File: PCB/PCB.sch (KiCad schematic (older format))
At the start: 151 parts

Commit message: Updated the PCB schematic.
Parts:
- removed D? (x8): 1N4148, symbol Device:D_Small_ALT
- removed SW?: SW_0-12, symbol Switch:SW_MEC_5G
- removed SW? (x3): SW_0-13, symbol Switch:SW_MEC_5G
- removed SW?: SW_0-2, symbol Switch:SW_MEC_5G
- removed SW?: SW_0-3, symbol Switch:SW_MEC_5G
- removed SW?: SW_0-5, symbol Switch:SW_MEC_5G
- removed SW?: SW_0-6, symbol Switch:SW_MEC_5G
- removed SW?: SW_0-7, symbol Switch:SW_MEC_5G
- added OL?: SSD1306, symbol kbd:OLED
- added SW?: ENCODER, symbol Device:Rotary_Encoder_Switch
- SW?: value SW_0-0 -> SW_1-0
- SW?: value SW_0-1 -> SW_1-1
- SW?: value SW_0-2 -> SW_1-2
- SW?: value SW_0-3 -> SW_1-3
- SW?: value SW_0-4 -> SW_1-4
- SW?: value SW_0-5 -> SW_1-5
- SW?: value SW_0-6 -> SW_1-6
- SW?: value SW_0-7 -> SW_1-7
- SW?: value SW_0-8 -> SW_1-8
- SW?: value SW_0-9 -> SW_1-9
- SW?: value SW_0-10 -> SW_1-10
- SW?: value SW_0-11 -> SW_1-11
- SW?: value SW_0-12 -> SW_1-12
- SW?: value SW_0-13 -> SW_1-13
- SW?: value SW_0-14 -> SW_1-14
- SW?: value SW_0-0 -> SW_2-0
- SW?: value SW_0-1 -> SW_2-1
- SW?: value SW_0-2 -> SW_2-2
- SW?: value SW_0-3 -> SW_2-3
- SW?: value SW_0-4 -> SW_2-4
- SW?: value SW_0-5 -> SW_2-5
- SW?: value SW_0-6 -> SW_2-6
- SW?: value SW_0-7 -> SW_2-7
- SW?: value SW_0-8 -> SW_2-8
- SW?: value SW_0-9 -> SW_2-9
- SW?: value SW_0-10 -> SW_2-10
- SW?: value SW_0-11 -> SW_2-11
- SW?: value SW_0-14 -> SW_2-14
- SW?: value SW_0-0 -> SW_3-0
- SW?: value SW_0-1 -> SW_3-1
- SW?: value SW_0-2 -> SW_3-3
- SW?: value SW_0-3 -> SW_3-3
- SW?: value SW_0-4 -> SW_3-4
- SW?: value SW_0-5 -> SW_3-5
- SW?: value SW_0-6 -> SW_3-6
- SW?: value SW_0-7 -> SW_3-7
- SW?: value SW_0-8 -> SW_3-8
- SW?: value SW_0-9 -> SW_3-9
- SW?: value SW_0-10 -> SW_3-10
- SW?: value SW_0-11 -> SW_3-11
- SW?: value SW_0-12 -> SW_3-12
- SW?: value SW_0-14 -> SW_3-14
- SW?: value SW_0-0 -> SW_4-0
- SW?: value SW_0-1 -> SW_4-1
- SW?: value SW_0-4 -> SW_4-4
- SW?: value SW_0-8 -> SW_4-8
- SW?: value SW_0-9 -> SW_4-9
- SW?: value SW_0-10 -> SW_4-10
- SW?: value SW_0-11 -> SW_4-11
- SW?: value SW_0-12 -> SW_4-12
- SW?: value SW_0-14 -> SW_4-14
- U?: value YAAJ_BlackPill_Part_Like -> STM32 BlackPill
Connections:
- net COL0: now also U?.19 (PB8)
- net COL1: now also U?.20 (PB9)
- net COL10: now also U?.31 (PB0)
- net COL11: now also U?.32 (PB1)
- net COL12: now also U?.33 (PB10)
- net COL13: now also U?.34 (PB11), SW?.S1
- net COL14: now also U?.6 (PA9)
- net COL2: now also U?.23 (PA0)
- net COL3: now also U?.24 (PA1)
- net COL4: now also U?.25 (PA2)
- net COL5: now also U?.26 (PA3)
- net COL6: now also U?.27 (PA4)
- net COL7: now also U?.28 (PA5)
- net COL8: now also U?.29 (PA6)
- net COL9: now also U?.30 (PA7)
- net ROW0: now also U?.13 (PB5)
- net ROW1: now also U?.12 (PB4)
- net ROW2: now also U?.11 (PB3); no longer D?.1 (K)
- net ROW3: now also D?.1 (K), U?.10 (PA15)
- net ROW4: now also U?.7 (PA10)
- net at U?.14 (PB6): now also OL?.2 (SCL)
- net at U?.15 (PB7): now also OL?.1 (SDA)
- net at U?.16 (3V3): now also OL?.3 (VCC)
- net at U?.17 (GND): now also OL?.4 (GND)
- net at U?.2 (PB13): now also SW?.B
- net at U?.3 (PB14): now also SW?.C
- net at U?.4 (PB15): now also SW?.A
- net at D?.2 (A): now also SW?.S2
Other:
- moved on the sheet: D?, SW?, U?

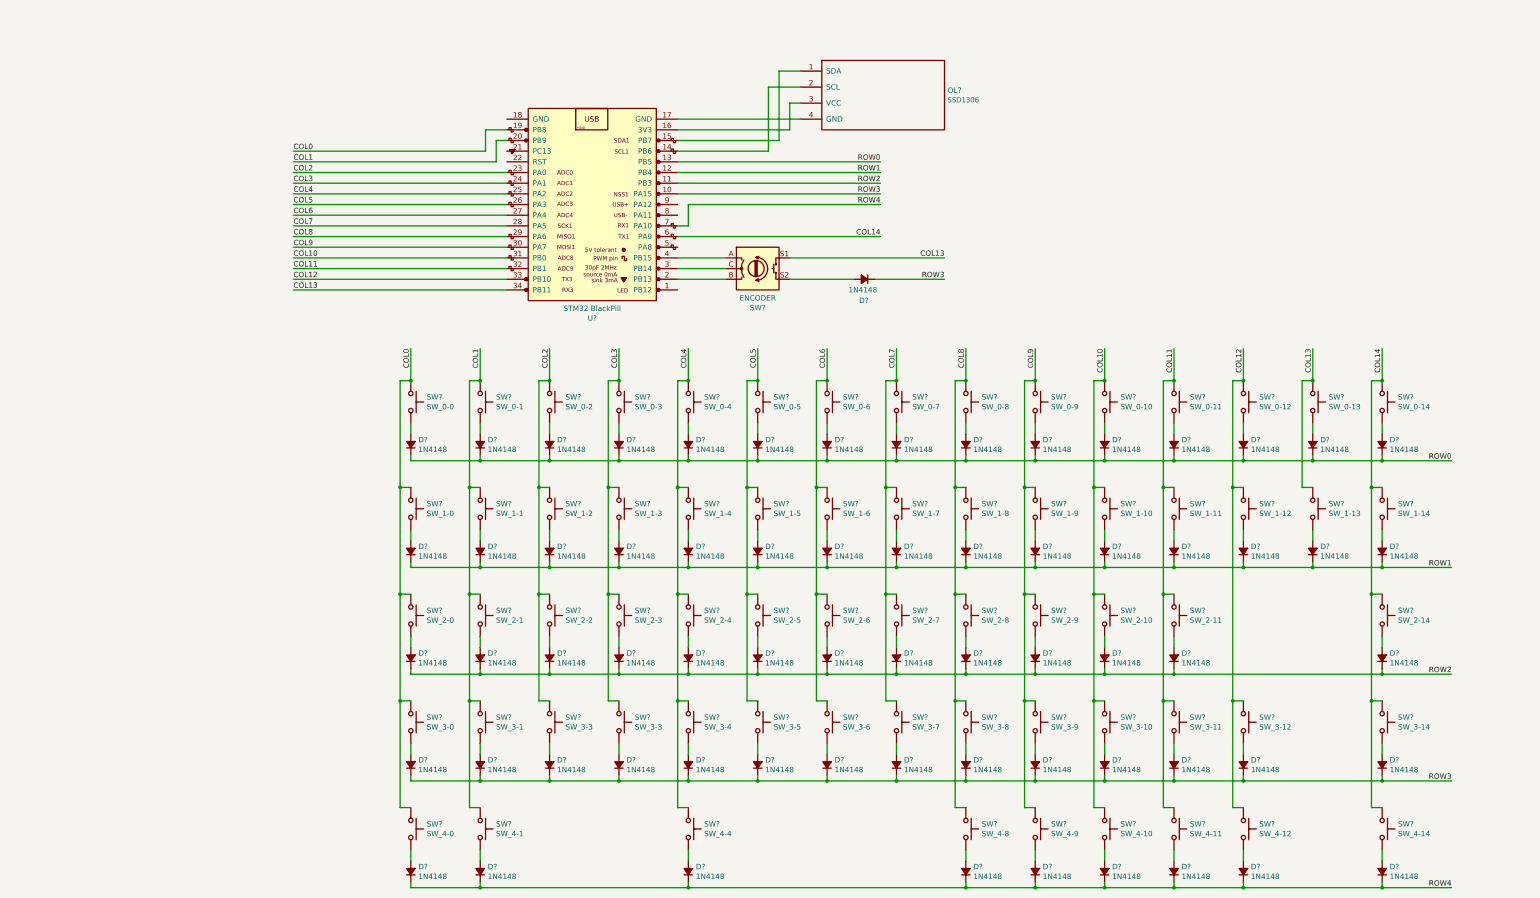
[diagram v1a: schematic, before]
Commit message: Updated the schematic, which should now be finished.
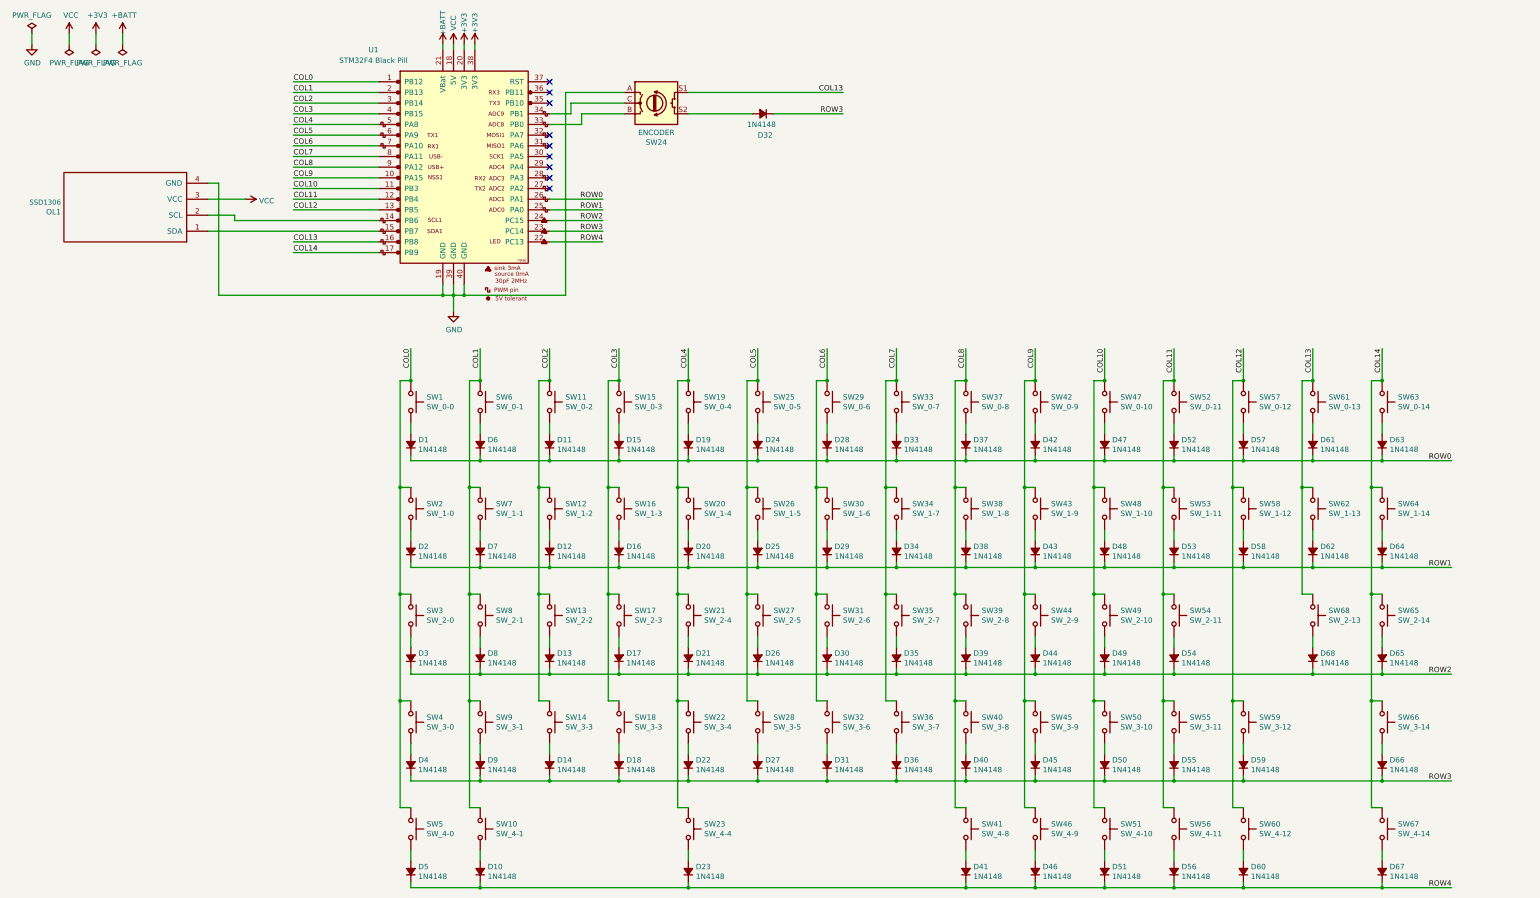
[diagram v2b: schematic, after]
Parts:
- removed U?: STM32 BlackPill, symbol YAAJ_BlackPill_Part_Like:YAAJ_BlackPill_Part_Like
- added D68: 1N4148, Diode_THT:D_DO-201_P12.70mm_Horizontal, symbol Device:D_Small_ALT
- added SW68: SW_2-13, Button_Switch_Keyboard:SW_Cherry_MX_2.25u_PCB, symbol Switch:SW_MEC_5G
- added U1: STM32F4 Black Pill, Footprints:YAAJ_BluePill_SWD_1, symbol YAAJ_BluePill:YAAJ_BluePill
- D1, D10, D11, D12, D13, D14, D15, D16, D17, D18, D19, D2, D20, D21, D22, D23, D24, D25, D26, D27, D28, D29, D3, D30, D31, D32, D33, D34, D35, D36, D37, D38, D39, D4, D40, D41, D42, D43, D44, D45, D46, D47, D48, D49, D5, D50, D51, D52, D53, D54, D55, D56, D57, D58, D59, D6, D60, D61, D62, D63, D64, D65, D66, D67, D7, D8, D9: renamed from D?; footprint (none) -> Diode_THT:D_DO-201_P12.70mm_Horizontal
- OL1: renamed from OL?; footprint (none) -> Connector_PinHeader_2.54mm:PinHeader_1x04_P2.54mm_Vertical
- SW1, SW10, SW11, SW12, SW13, SW14, SW15, SW16, SW17, SW18, SW19, SW20, SW21, SW22, SW25, SW26, SW27, SW28, SW29, SW30, SW31, SW32, SW33, SW34, SW35, SW36, SW37, SW38, SW39, SW40, SW42, SW43, SW44, SW45, SW47, SW48, SW49, SW50, SW52, SW53, SW54, SW56, SW57, SW58, SW59, SW6, SW60, SW63, SW64, SW65, SW66, SW67, SW7, SW8, SW9: renamed from SW?; footprint (none) -> Button_Switch_Keyboard:SW_Cherry_MX_1.00u_PCB
- SW2, SW5, SW62: renamed from SW?; footprint (none) -> Button_Switch_Keyboard:SW_Cherry_MX_1.50u_PCB
- SW23: renamed from SW?; footprint (none) -> Button_Switch_Keyboard:SW_Cherry_MX_6.25u_PCB
- SW24: renamed from SW?; footprint (none) -> Rotary_Encoder:RotaryEncoder_Alps_EC11E_Vertical_H20mm
- SW3, SW55: renamed from SW?; footprint (none) -> Button_Switch_Keyboard:SW_Cherry_MX_1.75u_PCB
- SW4: renamed from SW?; footprint (none) -> Button_Switch_Keyboard:SW_Cherry_MX_2.25u_PCB
- SW41, SW46, SW51: renamed from SW?; footprint (none) -> Button_Switch_Keyboard:SW_Cherry_MX_1.25u_PCB
- SW61: renamed from SW?; footprint (none) -> Button_Switch_Keyboard:SW_Cherry_MX_2.00u_PCB
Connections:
- net COL0: now also U1.1 (PB12)
- net COL1: now also U1.2 (PB13)
- net COL10: now also U1.11 (PB3)
- net COL11: now also U1.12 (PB4)
- net COL12: now also U1.13 (PB5)
- net COL13: now also SW68.1 (A), SW68.2 (A), U1.16 (PB8)
- net COL14: now also U1.17 (PB9)
- net COL2: now also U1.3 (PB14)
- net COL3: now also U1.4 (PB15)
- net COL4: now also U1.5 (PA8)
- net COL5: now also U1.6 (PA9)
- net COL6: now also U1.7 (PA10)
- net COL7: now also U1.8 (PA11)
- net COL8: now also U1.9 (PA12)
- net COL9: now also U1.10 (PA15)
- net ROW0: now also U1.26 (PA1)
- net ROW1: now also U1.25 (PA0)
- net ROW2: now also D68.1 (K), U1.24 (PC15)
- net ROW3: now also U1.23 (PC14)
- net ROW4: now also U1.22 (PC13)
- net at OL1.2 (SCL): now also U1.14 (PB6)
- net at OL1.1 (SDA): now also U1.15 (PB7)
- net VCC: now reaches OL1.3 (VCC)
- net VCC: now also U1.18 (5V)
- net GND: now reaches OL1.4 (GND)
- net GND: now also SW24.A, U1.19 (GND), U1.39 (GND), U1.40 (GND)
- net at SW24.B: now also U1.33 (PB0)
- net at SW24.C: now also U1.34 (PB1)
- new net: D68.2 (A), SW68.3 (B), SW68.4 (B)
- new net +3V3: U1.20 (3V3), U1.38 (3V3)
- new net +BATT: U1.21 (VBat)
- no-connect marks 0 -> 9
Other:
- moved on the sheet: D32, OL1, SW24
